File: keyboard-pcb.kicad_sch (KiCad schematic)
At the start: 0 parts

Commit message: Progressed microcontroller design
Atmega32u4 schematic work
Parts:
- added C1: 1uF, symbol Device:C_Small
- added C2, C3, C4: 0.1uF, symbol Device:C_Small
- added C5: 10uF, symbol Device:C_Small
- added C6, C7: 22pF, symbol Device:C_Small
- added J1: AVR-ISP-6, symbol Connector:AVR-ISP-6
- added R1, R4: 10k, symbol Device:R_Small
- added R2, R3: 22, symbol Device:R_Small
- added SW1: SW_Push, symbol Switch:SW_Push
- added U1: ATmega32U4-A, Package_QFP:TQFP-44_10x10mm_P0.8mm, symbol MCU_Microchip_ATmega:ATmega32U4-A
- added Y1: 16MHz, symbol Device:Crystal_GND24_Small
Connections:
- new net: C1.1, U1.6 (UCAP)
- new net: J1.1 (MISO), U1.11 (PB3)
- new net: J1.3 (SCK), U1.9 (PB1)
- new net: J1.4 (MOSI), U1.10 (PB2)
- new net: R3.2, U1.3 (D-)
- new net: C6.2, U1.16 (XTAL2), Y1.3
- new net: C7.2, U1.17 (XTAL1), Y1.1
- new net: R1.1, U1.33 (~{HWB}/PE2)
- new net: R2.1, U1.4 (D+)
- new net +5V: C2.1, C3.1, C4.1, C5.1, J1.2 (VCC), R4.1, U1.14 (VCC), U1.2 (UVCC), U1.24 (AVCC), U1.34 (VCC), U1.44 (AVCC), U1.7 (VBUS)
- new net D+: R2.2
- new net D-: R3.1
- new net GND: C1.2, C2.2, C3.2, C4.2, C5.2, C6.1, C7.1, J1.6 (GND), R1.2, SW1.1, U1.15 (GND), U1.23 (GND), U1.35 (GND), U1.43 (GND), U1.5 (UGND), Y1.2, Y1.4
- new net RST: J1.5 (~{RST}), R4.2, SW1.2, U1.13 (~{RESET})

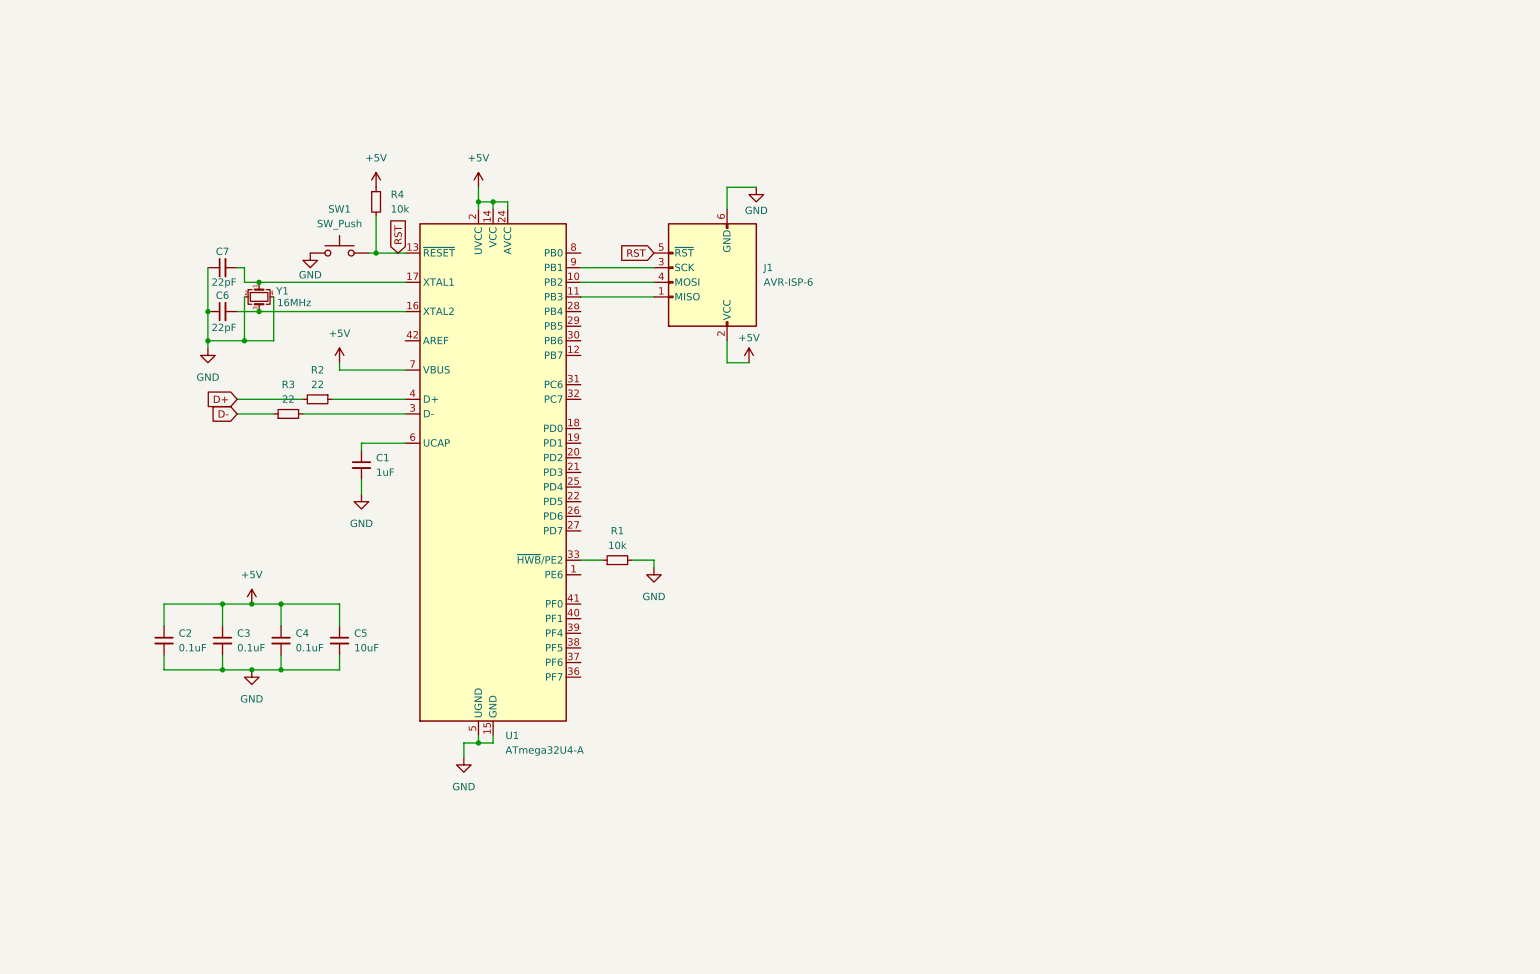
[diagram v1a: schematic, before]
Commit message: Constructed TKL keyswitch matrix
An 87 MX switch matrix with diodes
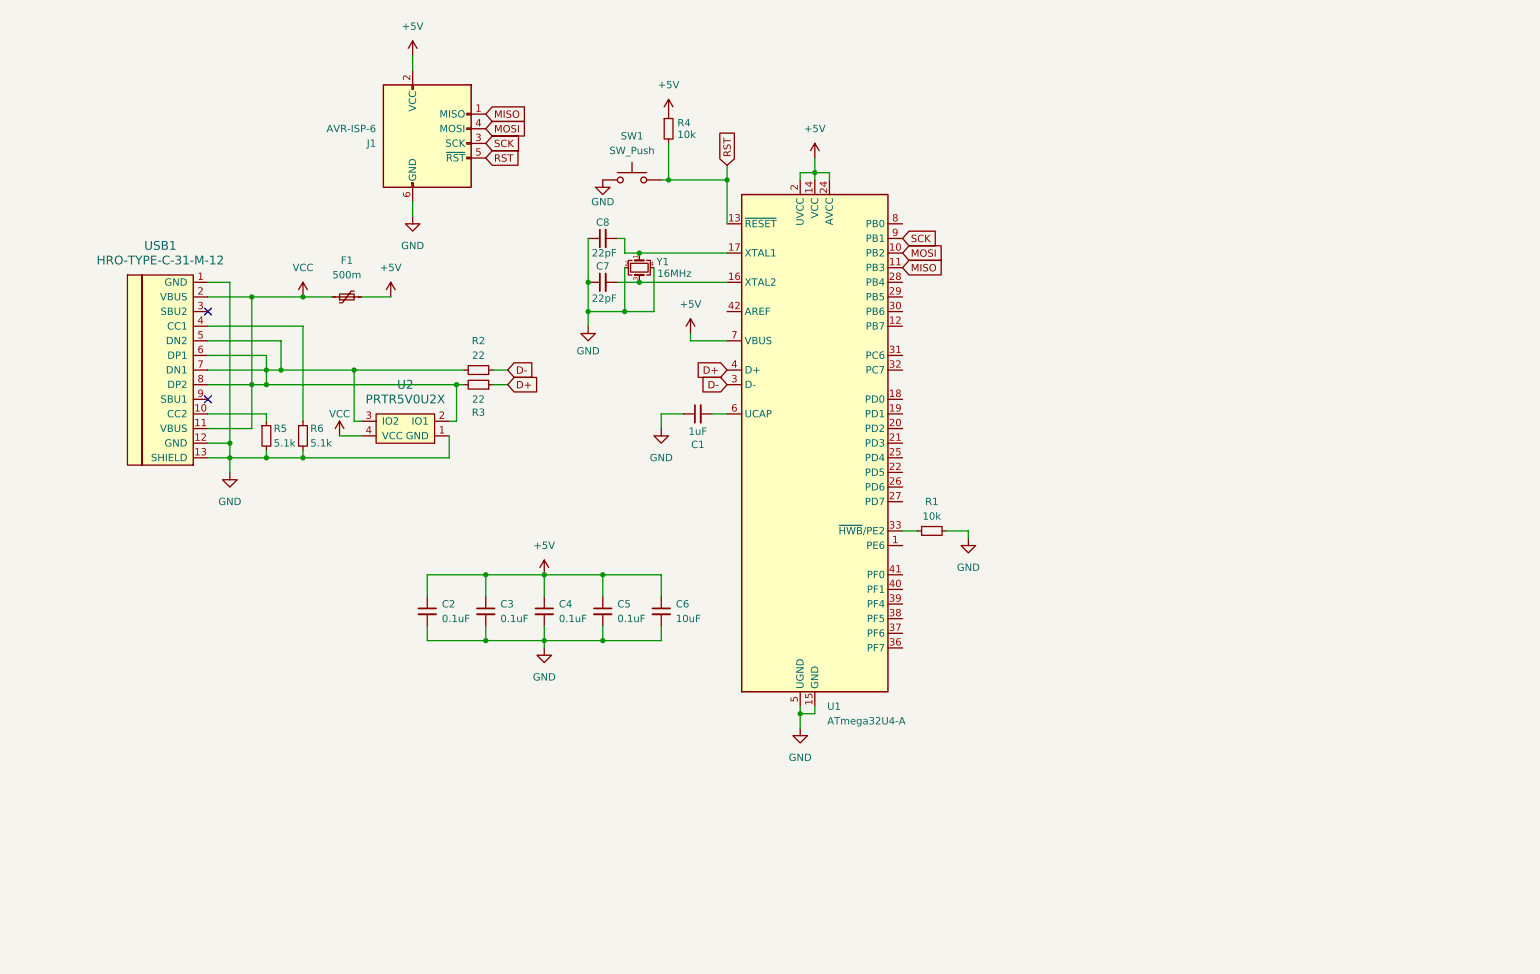
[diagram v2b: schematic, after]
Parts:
- added C2: 0.1uF, symbol Device:C_Small
- added F1: 500m, symbol Device:Polyfuse_Small
- added R5, R6: 5.1k, symbol Device:R_Small
- added U2: PRTR5V0U2X, symbol random-keyboard-parts:PRTR5V0U2X
- added USB1: HRO-TYPE-C-31-M-12, symbol Type-C:HRO-TYPE-C-31-M-12
- renumbered C2 to C3, C3 to C4, C4 to C5, C5 to C6, C6 to C7, C7 to C8
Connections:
- net +5V: now also C2.1, F1.2
- net D+: now also R3.1, U1.4 (D+); no longer R2.2
- net D-: now also R2.1, U1.3 (D-); no longer R3.1
- net GND: now also C1.1, C2.2, R5.2, R6.2, U2.1 (GND), USB1.1 (GND), USB1.12 (GND), USB1.13 (SHIELD); no longer C1.2
- net at U1.6 (UCAP): now also C1.2; no longer C1.1
- net MISO: now reaches J1.1 (MISO), U1.11 (PB3)
- net SCK: now reaches J1.3 (SCK), U1.9 (PB1)
- net MOSI: now reaches J1.4 (MOSI), U1.10 (PB2)
- net VCC: now reaches R3.2
- net VCC: now also R2.2, F1.1, U2.2 (IO1), U2.3 (IO2), U2.4 (VCC), USB1.11 (VBUS), USB1.2 (VBUS), USB1.5 (DN2), USB1.6 (DP1), USB1.7 (DN1), USB1.8 (DP2); no longer U1.3 (D-)
- new net: R6.1, USB1.4 (CC1)
- new net: R5.1, USB1.10 (CC2)
- no-connect marks 0 -> 2
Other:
- moved on the sheet: C1, C3, C4, C5, C6, C7, C8, J1, R1, R4, U1, Y1

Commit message: Add submodules
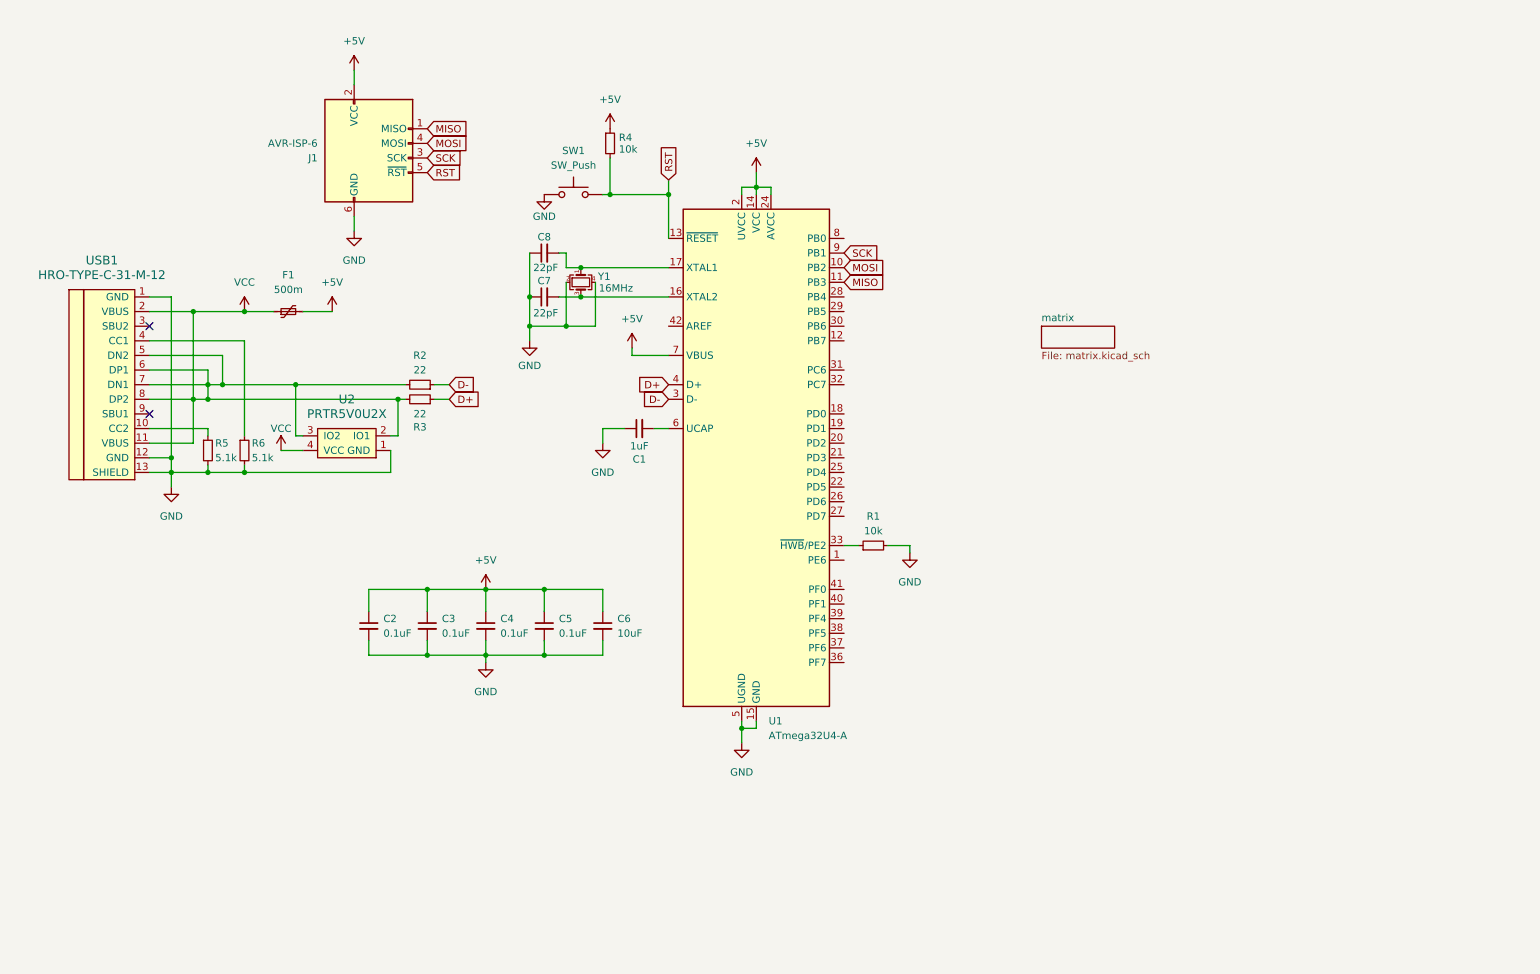
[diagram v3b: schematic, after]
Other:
- added sheet matrix (matrix.kicad_sch)
- moved on the sheet: C1, C2, C3, C4, C5, C6, C7, C8, F1, J1, R1, R2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

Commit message: Changed MCU circuitry
Atmega32u4 -> rp2040, updated USB-C connector, updated ESD protection, added memory chip, added voltage regulator
Tutorial followed: https://youtu.be/6Z49bynRqj8?si=SZUICHd2tr064eZg
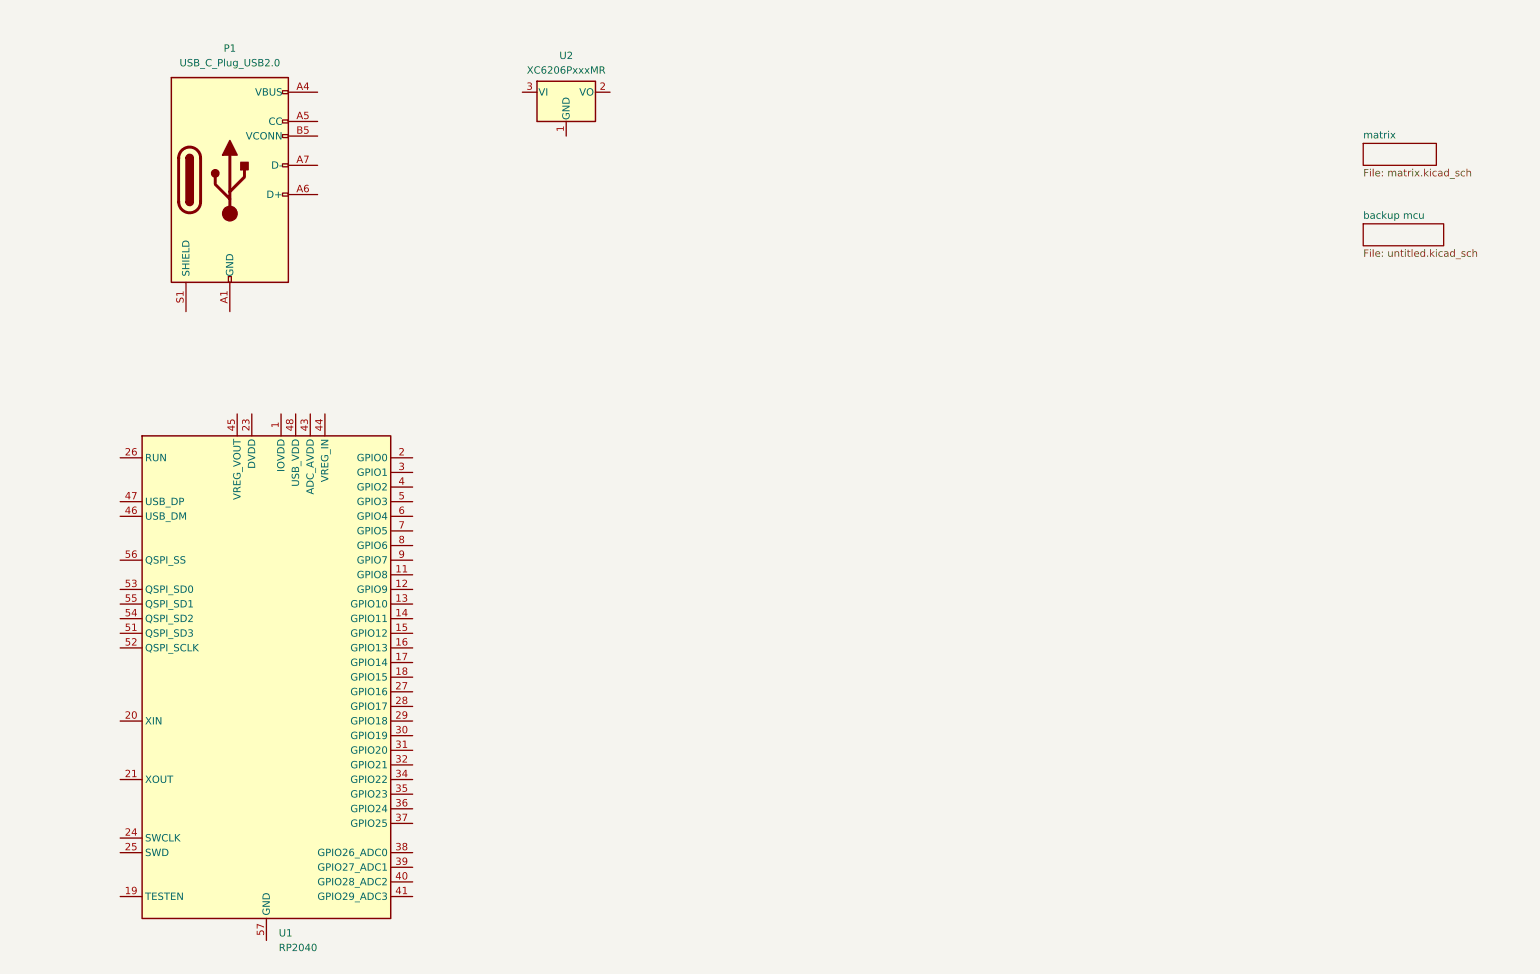
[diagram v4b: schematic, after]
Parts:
- removed C1: 1uF, symbol Device:C_Small
- removed C2, C3, C4, C5: 0.1uF, symbol Device:C_Small
- removed C6: 10uF, symbol Device:C_Small
- removed C7, C8: 22pF, symbol Device:C_Small
- removed F1: 500m, symbol Device:Polyfuse_Small
- removed J1: AVR-ISP-6, symbol Connector:AVR-ISP-6
- removed R1, R4: 10k, symbol Device:R_Small
- removed R2, R3: 22, symbol Device:R_Small
- removed R5, R6: 5.1k, symbol Device:R_Small
- removed SW1: SW_Push, symbol Switch:SW_Push
- removed U1: ATmega32U4-A, Package_QFP:TQFP-44_10x10mm_P0.8mm, symbol MCU_Microchip_ATmega:ATmega32U4-A
- removed U2: PRTR5V0U2X, symbol random-keyboard-parts:PRTR5V0U2X
- removed USB1: HRO-TYPE-C-31-M-12, symbol Type-C:HRO-TYPE-C-31-M-12
- removed Y1: 16MHz, symbol Device:Crystal_GND24_Small
- added P1: USB_C_Plug_USB2.0, symbol Connector:USB_C_Plug_USB2.0
- added U1: RP2040, Package_DFN_QFN:QFN-56-1EP_7x7mm_P0.4mm_EP3.2x3.2mm, symbol MCU_RaspberryPi:RP2040
- added U2: XC6206PxxxMR, Package_TO_SOT_SMD:SOT-23-3, symbol Regulator_Linear:XC6206PxxxMR
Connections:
- new net: U1.1 (IOVDD), U1.10 (IOVDD), U1.22 (IOVDD), U1.33 (IOVDD), U1.42 (IOVDD), U1.49 (IOVDD)
- new net: U1.23 (DVDD), U1.50 (DVDD)
- new net: P1.A1 (GND), P1.A12 (GND), P1.B1 (GND), P1.B12 (GND)
- new net: P1.A4 (VBUS), P1.A9 (VBUS), P1.B4 (VBUS), P1.B9 (VBUS)
- no-connect marks 2 -> 0
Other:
- added sheet backup mcu (untitled.kicad_sch)
